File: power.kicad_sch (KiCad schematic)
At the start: 53 parts, among them J10 Conn_01x02, J11 Solar_Cell, J2 USB_C_Receptacle_USB2.0_14P, J9 Battery_Cell, Q1 AO4882, Q3 AO4882, U2 BQ25798, U5 TPS6282x

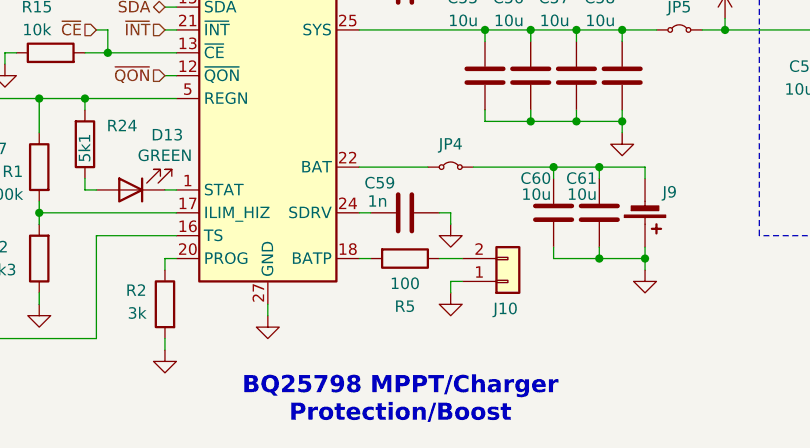
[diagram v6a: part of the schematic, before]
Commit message: schem: assign footprints
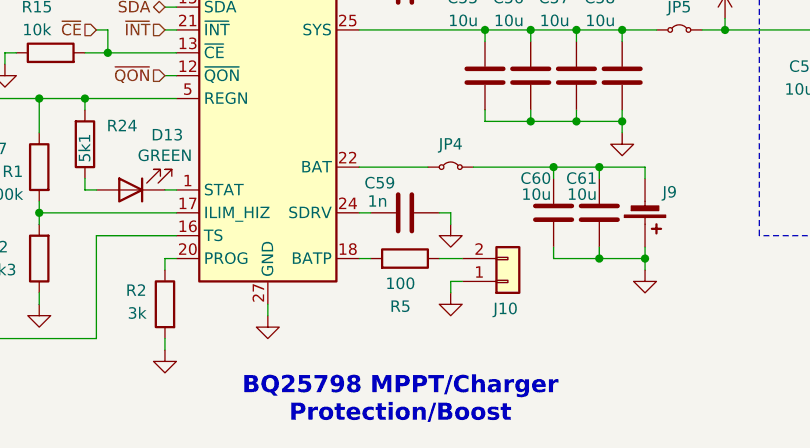
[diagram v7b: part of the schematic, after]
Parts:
- JP3, JP4, JP5: footprint (none) -> Connector_PinHeader_2.54mm:PinHeader_1x02_P2.54mm_Vertical
- R1, R2: footprint (none) -> Resistor_SMD:R_0402_1005Metric
- R5: footprint (none) -> Resistor_SMD:R_0402_1005Metric; Basic (none) -> Y; JLCPCB Part # (none) -> C25076; Manufacturer (none) -> Uniroyal Elec; Manufacturer Part Number (none) -> 0402WGF1000TCE
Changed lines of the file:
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@@
 			)
 		)
-		(property "Footprint" ""
+		(property "Footprint" "Resistor_SMD:R_0402_1005Metric"
 			(at 138.938 133.35 90)
 			(hide yes)
@@
 			)
 		)
-		(property "Footprint" ""
+		(property "Footprint" "Connector_PinHeader_2.54mm:PinHeader_1x02_P2.54mm_Vertical"
 			(at 82.55 85.09 0)
 			(hide yes)
@@
 			)
 		)
-		(property "Footprint" ""
+		(property "Footprint" "Connector_PinHeader_2.54mm:PinHeader_1x02_P2.54mm_Vertical"
 			(at 194.31 102.87 0)
 			(hide yes)
@@
 			)
 		)
-		(property "Footprint" ""
+		(property "Footprint" "Resistor_SMD:R_0402_1005Metric"
 			(at 124.968 118.11 90)
 			(hide yes)
@@
 			)
 		)
-		(property "Footprint" ""
+		(property "Footprint" "Connector_PinHeader_2.54mm:PinHeader_1x02_P2.54mm_Vertical"
 			(at 168.91 118.11 0)
 			(hide yes)
@@
 	)
 	(symbol
-		(lib_id "Device:Solar_Cell")
-		(at 76.2 88.9 180)
+		(lib_id "Device:R")
+		(at 163.83 128.27 270)
+		(mirror x)
 		(unit 1)
 		(body_style 1)
@@
 		(in_pos_files yes)
 		(dnp no)
-		(fields_autoplaced yes)
-		(property "Reference" "J11"
-			(at 72.39 91.0589 0)
+		(property "Reference" "R5"
+			(at 163.322 133.604 90)
 			(show_name no)
 			(do_not_autoplace no)
@@
 					(size 1.27 1.27)
 				)
-				(justify left)
 			)
 		)
-		(property "Value" "Solar_Cell"
-			(at 73.66 88.9 0)
-			(hide yes)
+		(property "Value" "100"
+			(at 163.322 131.064 90)
 			(show_name no)
 			(do_not_autoplace no)
@@
 					(size 1.27 1.27)
 				)
-				(justify left)
 			)
 		)
-		(property "Footprint" "Connector_JST:JST_XH_B2B-XH-A_1x02_P2.50mm_Vertical"
-			(at 76.2 90.424 90)
+		(property "Footprint" "Resistor_SMD:R_0402_1005Metric"
+			(at 163.83 130.048 90)
 			(hide yes)
 			(show_name no)
@@
 		)
 		(property "Datasheet" ""
-			(at 76.2 90.424 90)
+			(at 163.83 128.27 0)
 			(hide yes)
 			(show_name no)
@@
 			)
 		)
-		(property "Description" "Single solar cell"
-			(at 76.2 88.9 0)
+		(property "Description" "Resistor"
+			(at 163.83 128.27 0)
 			(hide yes)
 			(show_name no)
@@
 			)
 		)
-		(property "Basic" "Z"
-			(at 76.2 88.9 0)
+		(property "Basic" "Y"
+			(at 163.83 128.27 0)
 			(hide yes)
 			(show_name no)
@@
 			)
 		)
-		(property "JLCPCB Part #" "C158012"
-			(at 76.2 88.9 0)
+		(property "JLCPCB Part #" "C25076"
+			(at 163.83 128.27 0)
 			(hide yes)
 			(show_name no)
@@
 			)
 		)
-		(property "Manufacturer" "JST"
-			(at 76.2 88.9 0)
+		(property "Manufacturer" "Uniroyal Elec"
+			(at 163.83 128.27 0)
 			(hide yes)
 			(show_name no)
@@
 			)
 		)
-		(property "Manufacturer Part Number" "B2B-XH-A(LF)(SN)"
-			(at 76.2 88.9 0)
+		(property "Manufacturer Part Number" "0402WGF1000TCE"
+			(at 163.83 128.27 0)
 			(hide yes)
 			(show_name no)
@@
 			(project "carte-meteo-lora-1"
 				(path "/13f499c2-4dc3-4e2c-8cf4-c7d5e00eb573/9999b4d2-cbfb-4c4d-87a4-97a3463f3d3b"
-					(reference "J11")
+					(reference "R5")
 					(unit 1)
 				)
@@
 	)
 	(symbol
-		(lib_id "Device:R")
-		(at 124.46 105.41 90)
+		(lib_id "Device:Solar_Cell")
+		(at 76.2 88.9 180)
 		(unit 1)
 		(body_style 1)
@@
 		(in_pos_files yes)
 		(dnp no)
-		(property "Reference" "R15"
-			(at 122.936 100.33 90)
+		(fields_autoplaced yes)
+		(property "Reference" "J11"
+			(at 72.39 91.0589 0)
 			(show_name no)
 			(do_not_autoplace no)
@@
 					(size 1.27 1.27)
 				)
+				(justify left)
 			)
 		)
-		(property "Value" "10k"
-			(at 122.936 102.87 90)
+		(property "Value" "Solar_Cell"
+			(at 73.66 88.9 0)
+			(hide yes)
 			(show_name no)
 			(do_not_autoplace no)
@@
 					(size 1.27 1.27)
 				)
+				(justify left)
 			)
 		)
-		(property "Footprint" "Resistor_SMD:R_0402_1005Metric"
-			(at 124.46 107.188 90)
+		(property "Footprint" "Connector_JST:JST_XH_B2B-XH-A_1x02_P2.50mm_Vertical"
+			(at 76.2 90.424 90)
 			(hide yes)
 			(show_name no)
@@
 		)
 		(property "Datasheet" ""
-			(at 124.46 105.41 0)
+			(at 76.2 90.424 90)
 			(hide yes)
 			(show_name no)
@@
 			)
 		)
-		(property "Description" "Resistor"
-			(at 124.46 105.41 0)
+		(property "Description" "Single solar cell"
+			(at 76.2 88.9 0)
 			(hide yes)
 			(show_name no)
@@
 			)
 		)
-		(property "Basic" "Y"
-			(at 124.46 105.41 90)
+		(property "Basic" "Z"
+			(at 76.2 88.9 0)
 			(hide yes)
 			(show_name no)
@@
 			)
 		)
-		(property "JLCPCB Part #" "C25744"
-			(at 124.46 105.41 90)
+		(property "JLCPCB Part #" "C158012"
+			(at 76.2 88.9 0)
 			(hide yes)
 			(show_name no)
@@
 			)
 		)
-		(property "Manufacturer" "Uniroyal Elec"
-			(at 124.46 105.41 90)
+		(property "Manufacturer" "JST"
+			(at 76.2 88.9 0)
 			(hide yes)
 			(show_name no)
@@
 			)
 		)
-		(property "Manufacturer Part Number" "0402WGF1002TCE"
-			(at 124.46 105.41 90)
+		(property "Manufacturer Part Number" "B2B-XH-A(LF)(SN)"
+			(at 76.2 88.9 0)
 			(hide yes)
 			(show_name no)
@@
 			(project "carte-meteo-lora-1"
 				(path "/13f499c2-4dc3-4e2c-8cf4-c7d5e00eb573/9999b4d2-cbfb-4c4d-87a4-97a3463f3d3b"
-					(reference "R15")
+					(reference "J11")
 					(unit 1)
 				)
@@
 	(symbol
 		(lib_id "Device:R")
-		(at 163.83 128.27 270)
+		(at 124.46 105.41 90)
 		(unit 1)
 		(body_style 1)
@@
 		(in_pos_files yes)
 		(dnp no)
-		(property "Reference" "R5"
-			(at 163.83 133.604 90)
+		(property "Reference" "R15"
+			(at 122.936 100.33 90)
 			(show_name no)
 			(do_not_autoplace no)
@@
 			)
 		)
-		(property "Value" "100"
-			(at 163.83 131.064 90)
+		(property "Value" "10k"
+			(at 122.936 102.87 90)
 			(show_name no)
 			(do_not_autoplace no)
@@
 			)
 		)
-		(property "Footprint" ""
-			(at 163.83 126.492 90)
+		(property "Footprint" "Resistor_SMD:R_0402_1005Metric"
+			(at 124.46 107.188 90)
 			(hide yes)
 			(show_name no)
@@
 		)
 		(property "Datasheet" ""
-			(at 163.83 128.27 0)
+			(at 124.46 105.41 0)
 			(hide yes)
 			(show_name no)
@@
 		)
 		(property "Description" "Resistor"
-			(at 163.83 128.27 0)
+			(at 124.46 105.41 0)
+			(hide yes)
+			(show_name no)
+			(do_not_autoplace no)
+			(effects
+				(font
+					(size 1.27 1.27)
+				)
+			)
+		)
+		(property "Basic" "Y"
+			(at 124.46 105.41 90)
+			(hide yes)
+			(show_name no)
+			(do_not_autoplace no)
+			(effects
+				(font
+					(size 1.27 1.27)
+				)
+			)
+		)
+		(property "JLCPCB Part #" "C25744"
+			(at 124.46 105.41 90)
+			(hide yes)
+			(show_name no)
+			(do_not_autoplace no)
+			(effects
+				(font
+					(size 1.27 1.27)
+				)
+			)
+		)
+		(property "Manufacturer" "Uniroyal Elec"
+			(at 124.46 105.41 90)
+			(hide yes)
+			(show_name no)
+			(do_not_autoplace no)
+			(effects
+				(font
+					(size 1.27 1.27)
+				)
+			)
+		)
+		(property "Manufacturer Part Number" "0402WGF1002TCE"
+			(at 124.46 105.41 90)
 			(hide yes)
 			(show_name no)
@@
 			(project "carte-meteo-lora-1"
 				(path "/13f499c2-4dc3-4e2c-8cf4-c7d5e00eb573/9999b4d2-cbfb-4c4d-87a4-97a3463f3d3b"
-					(reference "R5")
+					(reference "R15")
 					(unit 1)
 				)

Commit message: schem: add ordering info to BOM
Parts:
- C6, C8: footprint Capacitor_SMD:C_0402_1005Metric -> Capacitor_SMD:C_0603_1608Metric; Basic (none) -> Y; JLCPCB Part # (none) -> C1622; Manufacturer (none) -> Samsung Electro-Mechanics; Manufacturer Part Number (none) -> CL10B473KB8NNNC
- C7: Basic (none) -> Y; JLCPCB Part # (none) -> C19666; Manufacturer (none) -> Samsung Electro-Mechanics; Manufacturer Part Number (none) -> CL10A475KO8NNNC
- L5: footprint (none) -> Inductor_SMD:L_Changjiang_FXL0420; Basic (none) -> X; JLCPCB Part # (none) -> C167203; Manufacturer (none) -> cjiang; Manufacturer Part Number (none) -> FXL0420-1R0-M
- Q1, Q3: Basic (none) -> X; JLCPCB Part # (none) -> C3040598; Manufacturer (none) -> TECH PUBLIC; Manufacturer Part Number (none) -> AO4882
- R1: Basic (none) -> Y; JLCPCB Part # (none) -> C25741; Manufacturer (none) -> Uniroyal Elec; Manufacturer Part Number (none) -> 0402WGF1003TCE
- R2: footprint Resistor_SMD:R_0402_1005Metric -> Resistor_SMD:R_0603_1608Metric; Basic (none) -> Y; JLCPCB Part # (none) -> C4211; Manufacturer (none) -> Uniroyal Elec; Manufacturer Part Number (none) -> 0603WAF3001T5E
- U2: Basic (none) -> X; JLCPCB Part # (none) -> C2876593; Manufacturer (none) -> Texas Instruments; Manufacturer Part Number (none) -> BQ25798RQMR
